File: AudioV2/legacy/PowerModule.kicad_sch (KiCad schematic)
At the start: 15 parts, among them J201 +15/A_GND/-15 out, J202 PD module in (1=GND 2=+12V), U201 REC20K-2415DZ, U202 L7809CV +9V

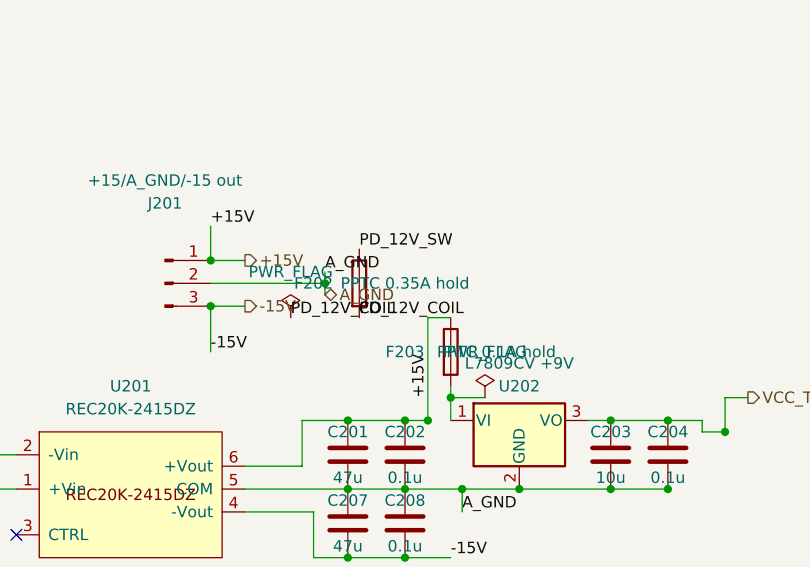
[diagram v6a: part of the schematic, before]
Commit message: AudioV2: ヒューズ / PPTC を入手性で型番決めし、5 個の FP を軸リードから実物に差し替えた
査読の指摘「F201 は Value 5×20 なのに FP が軸リード。他の 4 個も同じ」を潰した。

- 5×20 ガラス管（F201 T1.6A、F1601 T1A）: ホルダ Schurter OGN 0031.8201（DigiKey 在庫 6 万・¥240）。
  FP は KiCad 標準 Fuseholder_Cylinder-5x20mm_Schurter_0031_8201_Horizontal_Open
- PPTC（F202 / F203 / F1602）: Littelfuse RXEF040 / RXEF010 / RXEF050（在庫 2〜8 万）。
  Bourns MF-R040 / 010 / 050 も同寸で挿さる。F202 は 0.35 A の品が両社に無いので 0.40 A に寄せた
  （コイル枝のピークは約 0.16 A）。FP は Library:PPTC_Radial_D7.9mm_T3.1mm_P5.08mm を新設
  （DigiKey パラメータ: φ7.4〜7.9 × 3.0〜3.1、リード間隔 5.05 / 5.10。メーカー DS は 403 で未取得。
  穴 1.1 でピッチの差を吸収）
- 各 F の Description に型番と理由、PARTS.md の手書き行と NOW.md を更新

検証: 再生成バイト一致・check_sexpr 0（新 FP も）・kicad-cli fp export で FP 読込 OK・roundtrip OK・
ERC 11 件（変化なし）・部品 389・重複 0・フットプリント未設定 0

Co-Authored-By: Claude Fable 5.1 <noreply@anthropic.com>
Claude-Session: https://claude.ai/code/session_01VCArLcCGbMGgxvWJ5HFJiY
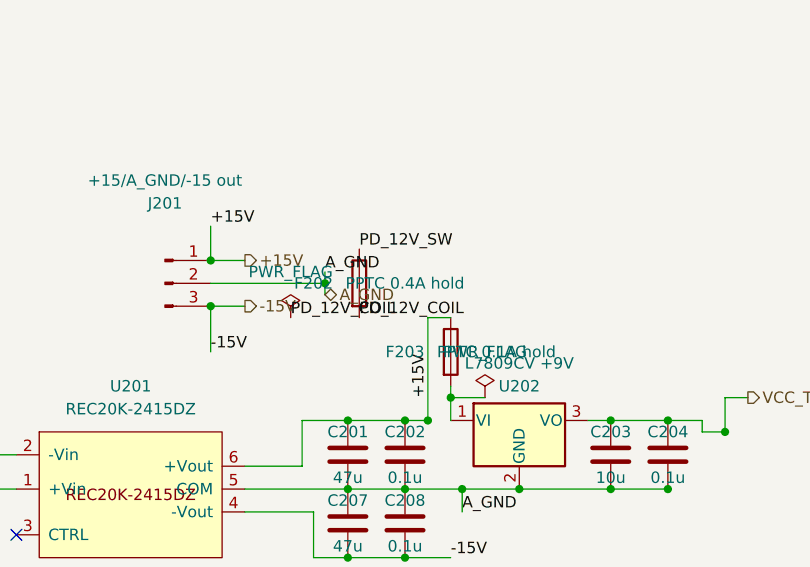
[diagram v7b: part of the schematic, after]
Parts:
- F201: footprint Resistor_THT:R_Axial_DIN0411_L9.9mm_D3.6mm_P12.70mm_Horizontal -> Fuse:Fuseholder_Cylinder-5x20mm_Schurter_0031_8201_Horizontal_Open
- F202: value PPTC 0.35A hold -> PPTC 0.4A hold; footprint Resistor_THT:R_Axial_DIN0411_L9.9mm_D3.6mm_P12.70mm_Horizontal -> Library:PPTC_Radial_D7.9mm_T3.1mm_P5.08mm
- F203: footprint Resistor_THT:R_Axial_DIN0411_L9.9mm_D3.6mm_P12.70mm_Horizontal -> Library:PPTC_Radial_D7.9mm_T3.1mm_P5.08mm
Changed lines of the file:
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@@
 			)
 		)
-		(property "Footprint" "Resistor_THT:R_Axial_DIN0411_L9.9mm_D3.6mm_P12.70mm_Horizontal"
+		(property "Footprint" "Fuse:Fuseholder_Cylinder-5x20mm_Schurter_0031_8201_Horizontal_Open"
 			(at -12.7 45.72 0)
 			(hide yes)
@@
 			)
 		)
-		(property "Description" ""
+		(property "Description" "入口ヒューズ（PD 12V → U201 REC20K）。ホルダは Schurter OGN 0031.8201（基板用 5×20 オープン型、DigiKey 在庫 6 万・¥240、KiCad 標準 FP）。中身は 5×20 ガラス管スローブロー T1.6A（例: Bel 0652C1000/1600-11、Littelfuse 0218 系、秋月の 5.2×20 スロー品も挿さる）。2026-09-09 に軸リード FP からホルダ FP へ直した"
 			(at -12.7 45.72 0)
 			(hide yes)
@@
 			)
 		)
-		(property "Value" "PPTC 0.35A hold"
+		(property "Value" "PPTC 0.4A hold"
 			(at 142.24 62.23 0)
 			(show_name no)
@@
 			)
 		)
-		(property "Footprint" "Resistor_THT:R_Axial_DIN0411_L9.9mm_D3.6mm_P12.70mm_Horizontal"
+		(property "Footprint" "Library:PPTC_Radial_D7.9mm_T3.1mm_P5.08mm"
 			(at -12.7 45.72 0)
 			(hide yes)
@@
 			)
 		)
-		(property "Description" ""
+		(property "Description" "リレーコイル電源（U403 前）の PPTC。0.35 A の品は Littelfuse/Bourns とも無いので 0.40 A に寄せた（コイル枝のピークは約 0.16 A）。ラジアル PPTC。Littelfuse RXEF040（Ih 0.40 A / It 0.80 A / 72 V）。Bourns MF-R040 も同寸で可。FP は DigiKey の寸法（φ7.4〜7.9×3.1、ピッチ 5.05〜5.10）から起こした Library の自作。2026-09-09 に軸リード FP から直した"
 			(at -12.7 45.72 0)
 			(hide yes)
@@
 			)
 		)
-		(property "Footprint" "Resistor_THT:R_Axial_DIN0411_L9.9mm_D3.6mm_P12.70mm_Horizontal"
+		(property "Footprint" "Library:PPTC_Radial_D7.9mm_T3.1mm_P5.08mm"
 			(at -12.7 45.72 0)
 			(hide yes)
@@
 			)
 		)
-		(property "Description" ""
+		(property "Description" "+9V LDO（U202）入口の PPTC。ラジアル PPTC。Littelfuse RXEF010（Ih 0.10 A / It 0.20 A / 60 V）。Bourns MF-R010 も同寸で可。FP は DigiKey の寸法（φ7.4〜7.9×3.1、ピッチ 5.05〜5.10）から起こした Library の自作。2026-09-09 に軸リード FP から直した"
 			(at -12.7 45.72 0)
 			(hide yes)

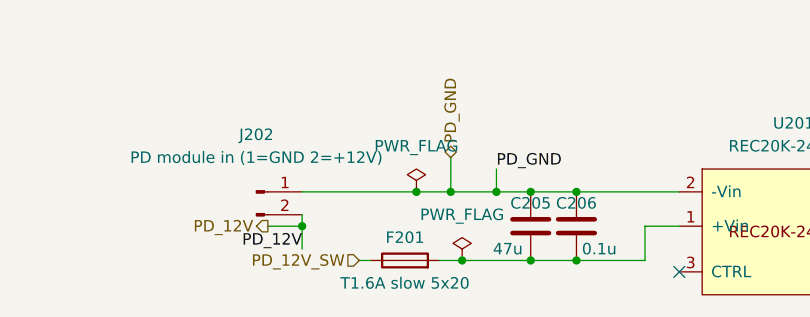
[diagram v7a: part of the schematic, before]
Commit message: AudioV2: F201 を F2A 速断に（定格上げなら突入猶予は不要）
T1.6A スローから上げたので、秋月で揃う速断 F2A（MF51NR 系）に合わせた。

Co-authored-by: Cursor <cursoragent@cursor.com>
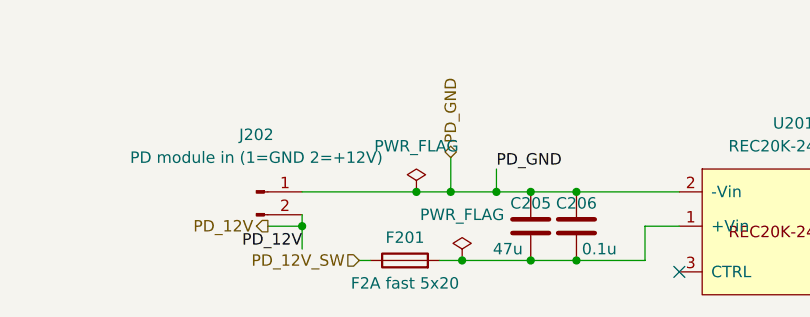
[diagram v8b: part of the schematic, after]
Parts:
- F201: value T1.6A slow 5x20 -> F2A fast 5x20
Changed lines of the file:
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@@
 			)
 		)
-		(property "Value" "T1.6A slow 5x20"
+		(property "Value" "F2A fast 5x20"
 			(at 68.58 91.44 90)
 			(show_name no)
@@
 			)
 		)
-		(property "Description" "入口ヒューズ（PD 12V → U201 REC20K）。ホルダは Schurter OGN 0031.8201（基板用 5×20 オープン型、DigiKey 在庫 6 万・¥240、KiCad 標準 FP）。中身は 5×20 ガラス管スローブロー T1.6A（例: Bel 0652C1000/1600-11、Littelfuse 0218 系、秋月の 5.2×20 スロー品も挿さる）。2026-09-09 に軸リード FP からホルダ FP へ直した"
+		(property "Description" "入口ヒューズ（PD 12V → U201 REC20K）。ホルダは Schurter OGN 0031.8201（基板用 5×20 オープン型、KiCad 標準 FP）。中身は 5×20 ガラス管速断 F2A（例: 秋月 MF51NR 250V2A / Littelfuse 0217.002HXP 系）。ホルダ FP は 2026-09-09。定格は入手性で T1.6A スロー→F2A 速断（2026-09-09）"
 			(at -12.7 45.72 0)
 			(hide yes)
